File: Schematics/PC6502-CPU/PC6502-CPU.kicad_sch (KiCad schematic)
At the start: 62 parts, among them J1 BUS, J4 TEST, J5 Conn_02x05_Odd_Even, J6 Conn_02x02_Odd_Even, U2 AS6C4008-55PCN, U3 SST39SF010, U4 ATF1504AS, U5 W65C02, U6 74AHC244, U8 MCP130-450DI/TO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

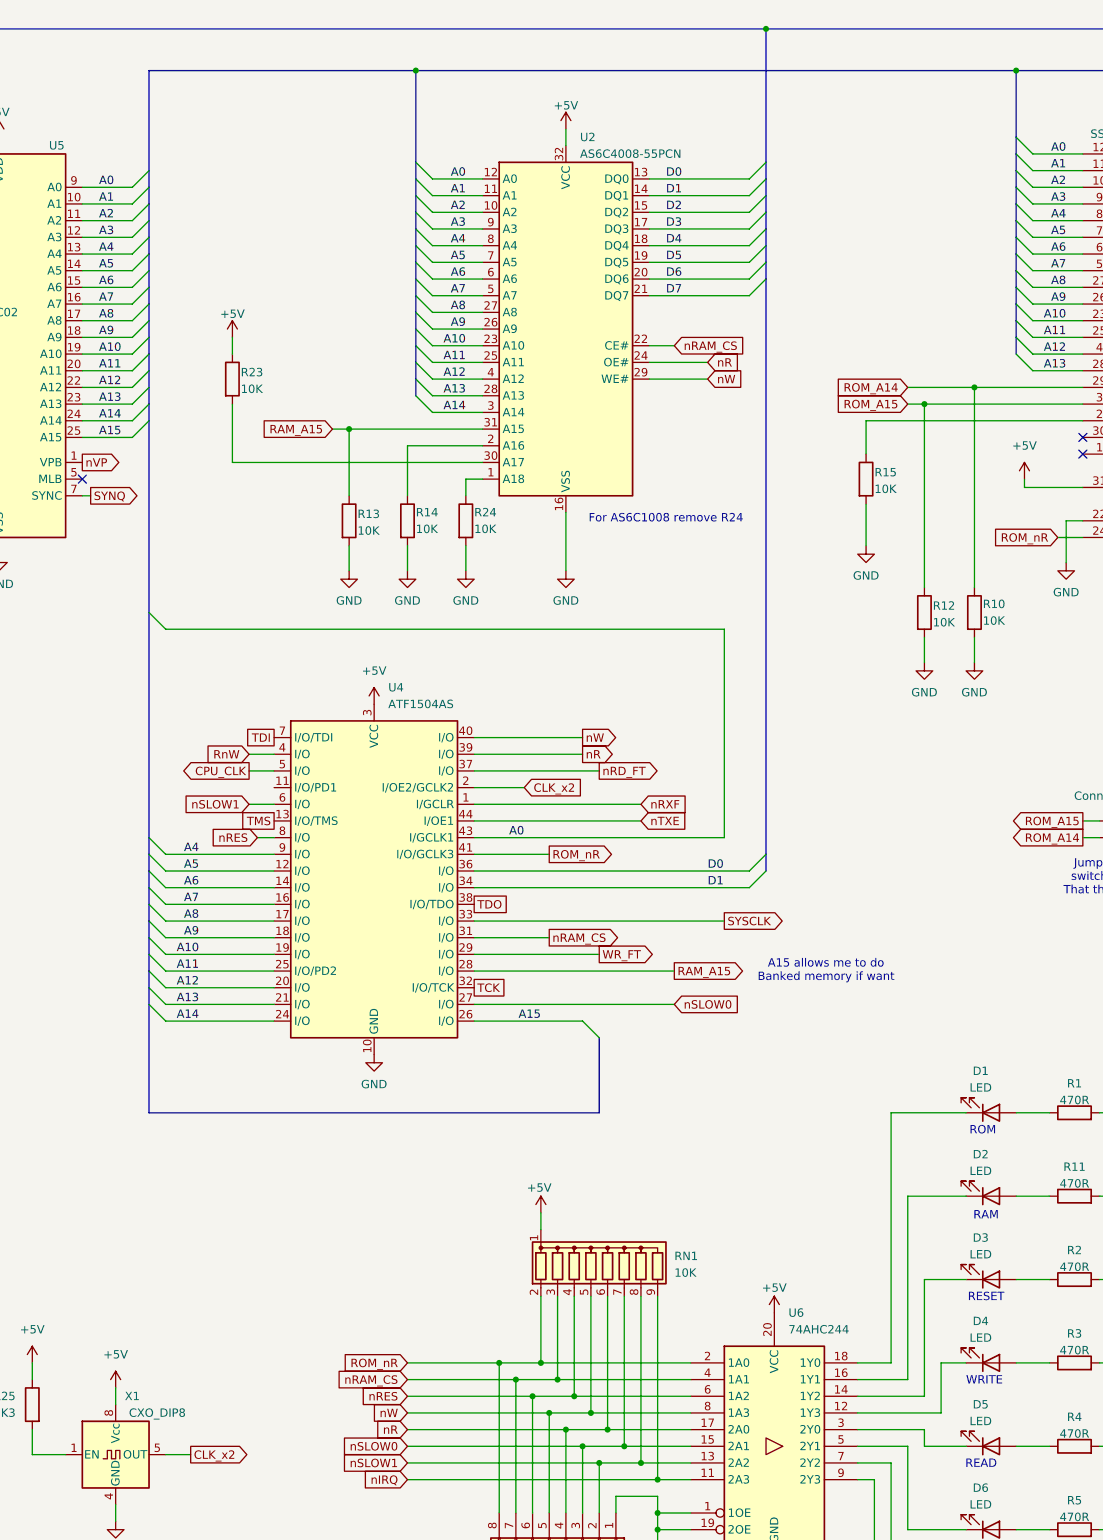
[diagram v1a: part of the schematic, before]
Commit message: Updated CPU to Rev 1.4
VErsion 1.4 of CPU board connects A15 direct to RAM and should allow me to get more than 32K of RAM available.
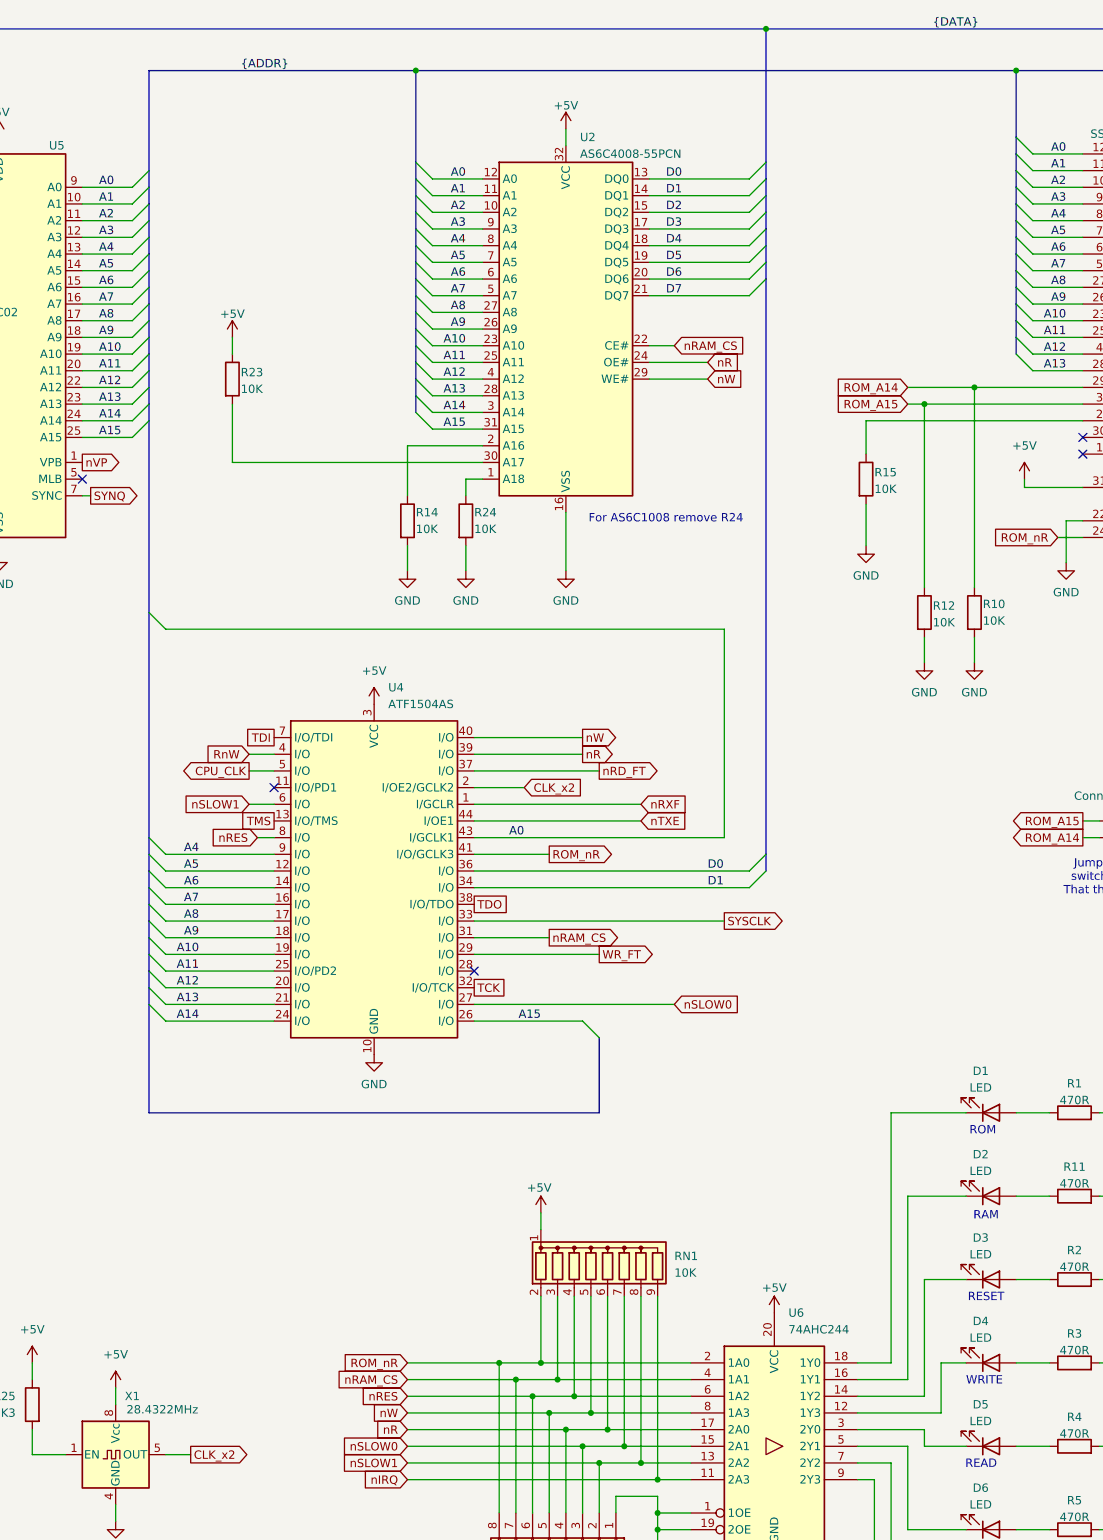
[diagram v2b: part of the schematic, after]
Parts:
- removed R13: 10K, Resistor_SMD:R_0603_1608Metric_Pad0.98x0.95mm_HandSolder, symbol Device:R
- X1: value CXO_DIP8 -> 28.4322MHz
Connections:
- net A15: now also U2.31 (A15)
- net RAM_A15: no longer names the net of U4.28 (I/O)
- net RAM_A15: no longer U2.31 (A15)
- no-connect marks 8 -> 10
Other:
- note removed: "A15 allows me to do Banked memory if want"
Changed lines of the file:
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@@
 		)
 	)
-	(text "A15 allows me to do\nBanked memory if want"
-		(exclude_from_sim no)
-		(at 225.044 162.56 0)
-		(effects
-			(font
-				(size 1.27 1.27)
-			)
-		)
-	)
 	(text "CPU_CLK is the stretched\nversion of CLK. \nUse nSLOW0 and nSLOW1 to\nslow the clock down"
 		(exclude_from_sim no)
@@
 	)
 	(junction
-		(at 152.4 80.01)
-		(diameter 0)
-		(color 0 0 0 0)
-	)
-	(junction
 		(at 240.03 76.2)
 		(diameter 0)
@@
 	)
 	(no_connect
+		(at 140.97 134.62)
+	)
+	(no_connect
 		(at 64.77 152.4)
 	)
@@
 	)
 	(no_connect
+		(at 171.45 162.56)
+	)
+	(no_connect
 		(at 64.77 149.86)
 	)
@@
 	)
 	(bus_entry
+		(at 165.1 80.01)
+		(size -2.54 -2.54)
+		(stroke
+			(width 0)
+			(type default)
+		)
+	)
+	(bus_entry
 		(at 124.46 110.49)
 		(size -2.54 -2.54)
@@
 	(wire
 		(pts
-			(xy 152.4 101.6) (xy 152.4 97.79)
-		)
-		(stroke
-			(width 0)
-			(type default)
-		)
-	)
-	(wire
-		(pts
 			(xy 264.16 38.1) (xy 256.54 38.1)
 		)
@@
 	(wire
 		(pts
-			(xy 152.4 80.01) (xy 172.72 80.01)
-		)
-		(stroke
-			(width 0)
-			(type default)
-		)
-	)
-	(wire
-		(pts
 			(xy 270.51 273.05) (xy 266.7 273.05)
 		)
@@
 	(wire
 		(pts
-			(xy 152.4 80.01) (xy 152.4 90.17)
-		)
-		(stroke
-			(width 0)
-			(type default)
-		)
-	)
-	(wire
-		(pts
 			(xy 124.46 157.48) (xy 140.97 157.48)
 		)
@@
 	(bus
 		(pts
+			(xy 162.56 74.93) (xy 162.56 77.47)
+		)
+		(stroke
+			(width 0)
+			(type default)
+		)
+	)
+	(bus
+		(pts
 			(xy 327.66 129.54) (xy 327.66 132.08)
 		)
@@
 	(wire
 		(pts
-			(xy 171.45 162.56) (xy 201.93 162.56)
-		)
-		(stroke
-			(width 0)
-			(type default)
-		)
-	)
-	(wire
-		(pts
 			(xy 116.84 243.84) (xy 116.84 246.38)
 		)
@@
 		)
 	)
-	(wire
-		(pts
-			(xy 149.86 80.01) (xy 152.4 80.01)
-		)
-		(stroke
-			(width 0)
-			(type default)
-		)
-	)
 	(bus
 		(pts
@@
 	(wire
 		(pts
+			(xy 172.72 80.01) (xy 165.1 80.01)
+		)
+		(stroke
+			(width 0)
+			(type default)
+		)
+	)
+	(wire
+		(pts
 			(xy 86.36 43.18) (xy 71.12 43.18)
 		)
@@
 		)
 	)
+	(label "A15"
+		(at 170.18 80.01 180)
+		(effects
+			(font
+				(size 1.27 1.27)
+			)
+			(justify right bottom)
+		)
+	)
 	(label "A7"
 		(at 326.39 154.94 180)
@@
 		)
 	)
+	(label "{ADDR}"
+		(at 135.89 25.4 0)
+		(effects
+			(font
+				(size 1.27 1.27)
+			)
+			(justify left bottom)
+		)
+	)
 	(label "A3"
 		(at 114.3 50.8 0)
@@
 		)
 	)
+	(label "{DATA}"
+		(at 241.3 19.05 0)
+		(effects
+			(font
+				(size 1.27 1.27)
+			)
+			(justify left bottom)
+		)
+	)
 	(label "D4"
 		(at 200.66 52.07 0)
@@
 		)
 	)
-	(global_label "RAM_A15"
-		(shape output)
-		(at 201.93 162.56 0)
-		(fields_autoplaced yes)
-		(effects
-			(font
-				(size 1.27 1.27)
-			)
-			(justify left)
-		)
-		(property "Intersheetrefs" "${INTERSHEET_REFS}"
-			(at 213.2004 162.56 0)
-			(effects
-				(font
-					(size 1.27 1.27)
-				)
-				(justify left)
-				(hide yes)
-			)
-		)
-	)
 	(global_label "ROM_nR"
 		(shape output)
@@
 		)
 	)
-	(global_label "RAM_A15"
-		(shape input)
-		(at 149.86 80.01 180)
-		(fields_autoplaced yes)
-		(effects
-			(font
-				(size 1.27 1.27)
-			)
-			(justify right)
-		)
-		(property "Intersheetrefs" "${INTERSHEET_REFS}"
-			(at 138.5896 80.01 0)
-			(effects
-				(font
-					(size 1.27 1.27)
-				)
-				(justify right)
-				(hide yes)
-			)
-		)
-	)
 	(global_label "nIRQ"
 		(shape input)
@@
 	)
 	(symbol
-		(lib_id "Device:R")
-		(at 152.4 93.98 0)
-		(unit 1)
-		(exclude_from_sim no)
-		(in_bom yes)
-		(on_board yes)
-		(dnp no)
-		(property "Reference" "R13"
-			(at 153.67 92.964 0)
-			(effects
-				(font
-					(size 1.27 1.27)
-				)
-				(justify left)
-			)
-		)
-		(property "Value" "10K"
-			(at 153.67 95.504 0)
-			(effects
-				(font
-					(size 1.27 1.27)
-				)
-				(justify left)
-			)
-		)
-		(property "Footprint" "Resistor_SMD:R_0603_1608Metric_Pad0.98x0.95mm_HandSolder"
-			(at 150.622 93.98 90)
-			(effects
-				(font
-					(size 1.27 1.27)
-				)
-				(hide yes)
-			)
-		)
-		(property "Datasheet" "~"
-			(at 152.4 93.98 0)
-			(effects
-				(font
-					(size 1.27 1.27)
-				)
-				(hide yes)
-			)
-		)
-		(property "Description" ""
-			(at 152.4 93.98 0)
-			(effects
-				(font
-					(size 1.27 1.27)
-				)
-			)
-		)
-		(property "LCSC" "C25744"
-			(at 152.4 93.98 0)
-			(effects
-				(font
-					(size 1.27 1.27)
-				)
-				(hide yes)
-			)
-		)
-		(pin "1"
-		)
-		(pin "2"
-		)
-		(instances
-			(project "PC6502-CPU"
-				(path "/f3365b77-bdc1-4fa0-8030-841dab6ab2be"
-					(reference "R13")
-					(unit 1)
-				)
-			)
-		)
-	)
-	(symbol
 		(lib_id "power:GND")
 		(at 67.31 204.47 0)
@@
 	)
 	(symbol
-		(lib_id "power:GND")
-		(at 152.4 101.6 0)
-		(unit 1)
-		(exclude_from_sim no)
-		(in_bom yes)
-		(on_board yes)
-		(dnp no)
-		(property "Reference" "#PWR058"
-			(at 152.4 107.95 0)
-			(effects
-				(font
-					(size 1.27 1.27)
-				)
-				(hide yes)
-			)
-		)
-		(property "Value" "GND"
-			(at 152.4 106.1625 0)
-			(effects
-				(font
-					(size 1.27 1.27)
-				)
-			)
-		)
-		(property "Footprint" ""
-			(at 152.4 101.6 0)
-			(effects
-				(font
-					(size 1.27 1.27)
-				)
-				(hide yes)
-			)
-		)
-		(property "Datasheet" ""
-			(at 152.4 101.6 0)
-			(effects
-				(font
-					(size 1.27 1.27)
-				)
-				(hide yes)
-			)
-		)
-		(property "Description" ""
-			(at 152.4 101.6 0)
-			(effects
-				(font
-					(size 1.27 1.27)
-				)
-			)
-		)
-		(pin "1"
-		)
-		(instances
-			(project "PC6502-CPU"
-				(path "/f3365b77-bdc1-4fa0-8030-841dab6ab2be"
-					(reference "#PWR058")
-					(unit 1)
-				)
-			)
-		)
-	)
-	(symbol
 		(lib_id "Device:R")
 		(at 262.89 222.25 90)
@@
 			)
 		)
-		(property "Value" "CXO_DIP8"
-			(at 123.19 229.87 0)
+		(property "Value" "28.4322MHz"
+			(at 123.952 229.362 0)
 			(effects
 				(font

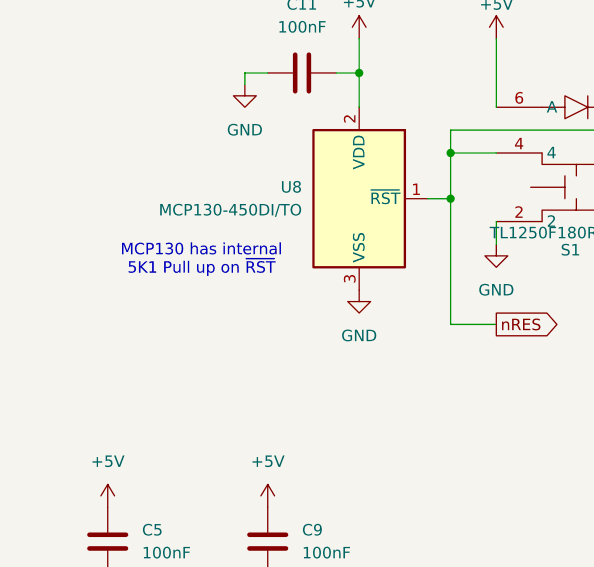
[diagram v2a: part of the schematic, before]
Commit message: Added basic tests for display, added transputer link adapter
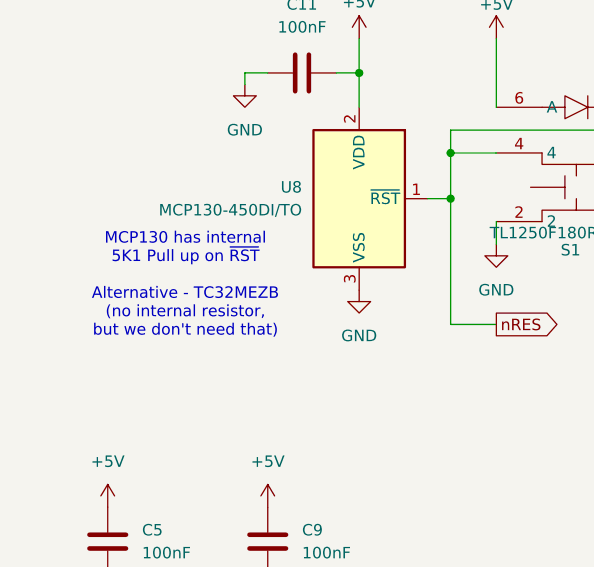
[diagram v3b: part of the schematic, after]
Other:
- note added: "MCP130 has internal 5K1 Pull up on ~{RST} Alternative - TC32MEZB (no internal resistor, but we don't need that)"
- note removed: "MCP130 has internal 5K1 Pull up on ~{RST}"
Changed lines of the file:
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@@
 		)
 	)
-	(text "MCP130 has internal\n5K1 Pull up on ~{RST}"
+	(text "MCP130 has internal\n5K1 Pull up on ~{RST}\n\nAlternative - TC32MEZB\n(no internal resistor,\nbut we don't need that)"
 		(exclude_from_sim no)
-		(at 34.544 206.248 0)
+		(at 32.766 209.042 0)
 		(effects
 			(font
